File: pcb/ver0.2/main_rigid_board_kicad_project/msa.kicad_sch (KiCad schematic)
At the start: 37 parts, among them J1 USB_A, J2 SWD Prog, U1 MCP1702, U3 W25Q128JV, U4 RP2040, Y1 H130B-12.000-20-3050-EXT-TR

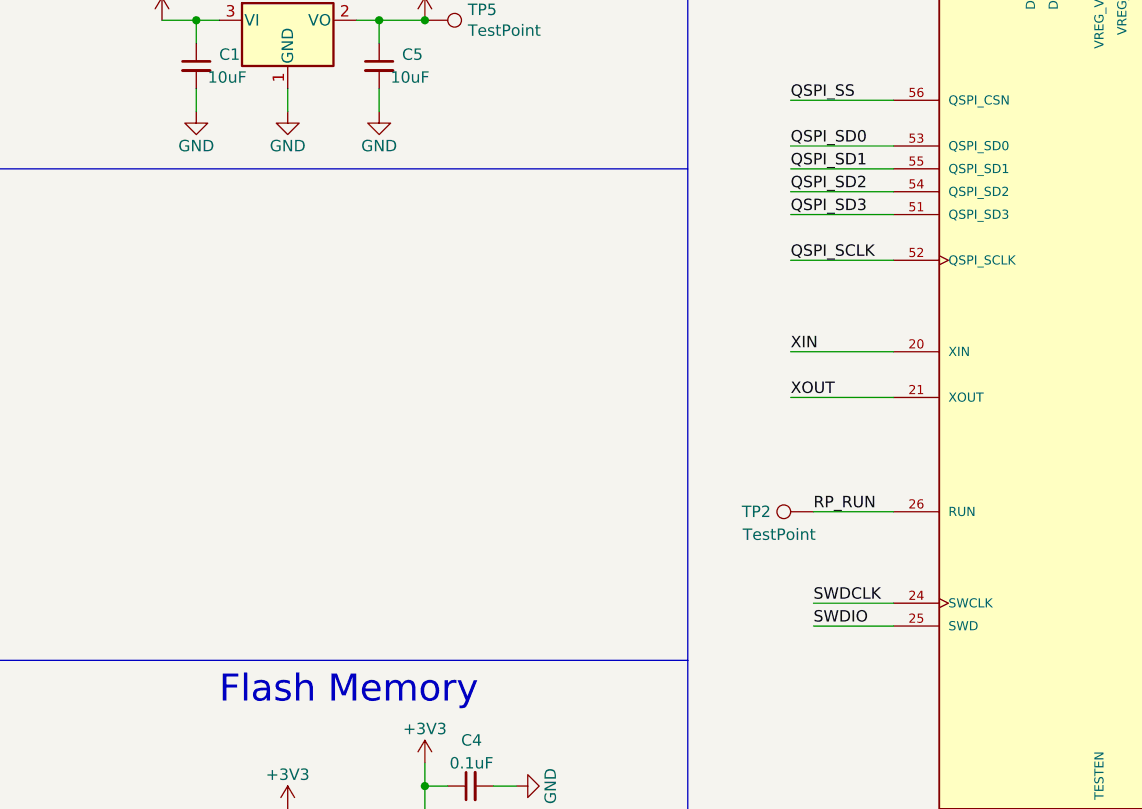
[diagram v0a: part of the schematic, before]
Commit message: add slimstack receptacle to library, add to main rigid board
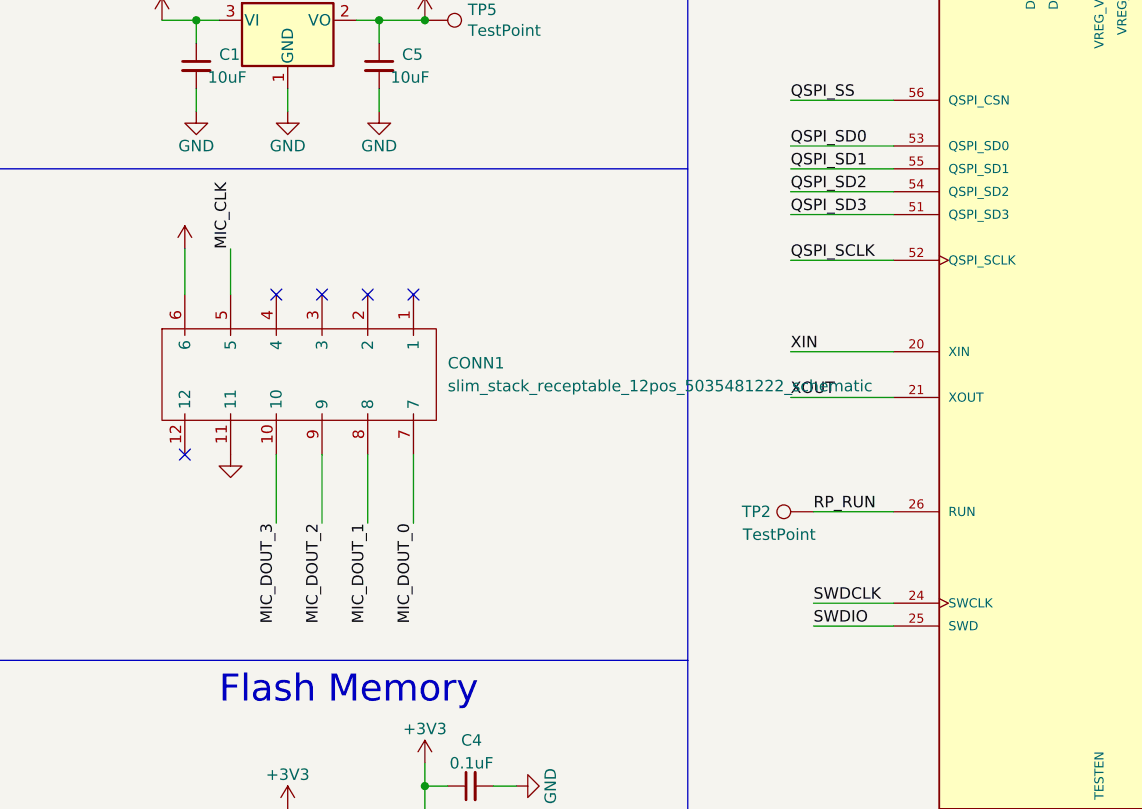
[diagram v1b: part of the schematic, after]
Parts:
- added CONN1: slim_stack_receptable_12pos_5035481222_schematic, OpenSourceSmartGlasses:slim_stack_molex_PLUG_5035521222, symbol MSA_lib:slim_stack_receptable_12pos_5035481222_schematic
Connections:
- net +3V3: now also CONN1.6
- net GND: now also CONN1.11
- net MIC_CLK: now also CONN1.5
- net MIC_DOUT_0: now also CONN1.7
- net MIC_DOUT_1: now also CONN1.8
- net MIC_DOUT_2: now also CONN1.9
- net MIC_DOUT_3: now also CONN1.10
- no-connect marks 24 -> 29
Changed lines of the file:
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@@
   (no_connect (at 182.88 105.41))
   (no_connect (at 182.88 130.81))
+  (no_connect (at 38.1 119.38))
   (no_connect (at 182.88 120.65))
   (no_connect (at 182.88 135.89))
   (no_connect (at 182.88 110.49))
+  (no_connect (at 63.5 101.6))
+  (no_connect (at 48.26 101.6))
+  (no_connect (at 58.42 101.6))
+  (no_connect (at 53.34 101.6))
   (no_connect (at 182.88 153.67))
   (no_connect (at 182.88 80.01))
@@
     (stroke (width 0) (type default) (color 0 0 0 0))
   )
+  (wire (pts (xy 63.5 119.38) (xy 63.5 127))
+    (stroke (width 0) (type default) (color 0 0 0 0))
+  )
   (polyline (pts (xy 172.72 162.56) (xy 236.22 162.56))
     (stroke (width 0) (type default) (color 0 0 0 0))
@@
     (stroke (width 0) (type default) (color 0 0 0 0))
   )
+  (wire (pts (xy 53.34 119.38) (xy 53.34 127))
+    (stroke (width 0) (type default) (color 0 0 0 0))
+  )
   (wire (pts (xy 59.69 71.12) (xy 64.77 71.12))
     (stroke (width 0) (type default) (color 0 0 0 0))
@@
     (stroke (width 0) (type default) (color 0 0 0 0))
   )
+  (wire (pts (xy 38.1 96.52) (xy 38.1 101.6))
+    (stroke (width 0) (type default) (color 0 0 0 0))
+  )
   (wire (pts (xy 257.81 120.65) (xy 257.81 123.19))
     (stroke (width 0) (type default) (color 0 0 0 0))
@@
     (stroke (width 0) (type default) (color 0 0 0 0))
   )
+  (wire (pts (xy 43.18 96.52) (xy 43.18 101.6))
+    (stroke (width 0) (type default) (color 0 0 0 0))
+  )
   (wire (pts (xy 182.88 69.85) (xy 193.04 69.85))
     (stroke (width 0) (type default) (color 0 0 0 0))
@@
     (stroke (width 0) (type default) (color 0 0 0 0))
   )
+  (wire (pts (xy 48.26 119.38) (xy 48.26 127))
+    (stroke (width 0) (type default) (color 0 0 0 0))
+  )
   (wire (pts (xy 116.84 135.89) (xy 107.95 135.89))
     (stroke (width 0) (type default) (color 0 0 0 0))
@@
   )
   (wire (pts (xy 182.88 138.43) (xy 193.04 138.43))
+    (stroke (width 0) (type default) (color 0 0 0 0))
+  )
+  (wire (pts (xy 58.42 119.38) (xy 58.42 127))
     (stroke (width 0) (type default) (color 0 0 0 0))
   )
@@
     (effects (font (size 1.27 1.27)) (justify left bottom))
   )
+  (label "MIC_CLK" (at 43.18 96.52 90)
+    (effects (font (size 1.27 1.27)) (justify left bottom))
+  )
   (label "XIN" (at 271.78 113.03 180)
     (effects (font (size 1.27 1.27)) (justify right bottom))
@@
     (effects (font (size 1.27 1.27)) (justify left bottom))
   )
+  (label "MIC_DOUT_3" (at 48.26 127 270)
+    (effects (font (size 1.27 1.27)) (justify right bottom))
+  )
   (label "QSPI_SCLK" (at 105.41 97.79 0)
     (effects (font (size 1.27 1.27)) (justify left bottom))
@@
   (label "MIC_DOUT_3" (at 193.04 140.97 0)
     (effects (font (size 1.27 1.27)) (justify left bottom))
+  )
+  (label "MIC_DOUT_2" (at 53.34 127 270)
+    (effects (font (size 1.27 1.27)) (justify right bottom))
   )
   (label "RED_LED" (at 194.31 133.35 180)
@@
     (effects (font (size 1.27 1.27)) (justify right bottom))
   )
+  (label "MIC_DOUT_1" (at 58.42 127 270)
+    (effects (font (size 1.27 1.27)) (justify right bottom))
+  )
   (label "MIC_CLK" (at 193.04 105.41 180)
     (effects (font (size 1.27 1.27)) (justify right bottom))
@@
   (label "SWDCLK" (at 251.46 83.82 0)
     (effects (font (size 1.27 1.27)) (justify left bottom))
+  )
+  (label "MIC_DOUT_0" (at 63.5 127 270)
+    (effects (font (size 1.27 1.27)) (justify right bottom))
   )
   (label "QSPI_SD0" (at 88.9 166.37 180)
@@
     (pin "1")
   )
+  (symbol (lib_name "GND_1") (lib_id "power:GND") (at 43.18 119.38 0) (unit 1)
+    (in_bom yes) (on_board yes) (fields_autoplaced)
+    (property "Reference" "#PWR05" (id 0) (at 43.18 125.73 0)
+      (effects (font (size 1.27 1.27)) hide)
+    )
+    (property "Value" "" (id 1) (at 43.18 124.46 0))
+    (property "Footprint" "" (id 2) (at 43.18 119.38 0)
+      (effects (font (size 1.27 1.27)) hide)
+    )
+    (property "Datasheet" "" (id 3) (at 43.18 119.38 0)
+      (effects (font (size 1.27 1.27)) hide)
+    )
+    (pin "1")
+  )
+  (symbol (lib_id "MSA_lib:slim_stack_receptable_12pos_5035481222_schematic") (at 44.45 107.95 0) (unit 1)
+    (in_bom yes) (on_board yes) (fields_autoplaced)
+    (property "Reference" "CONN1" (id 0) (at 67.31 109.2199 0)
+      (effects (font (size 1.27 1.27)) (justify left))
+    )
+    (property "Value" "slim_stack_receptable_12pos_5035481222_schematic" (id 1) (at 67.31 111.7599 0)
+      (effects (font (size 1.27 1.27)) (justify left))
+    )
+    (property "Footprint" "OpenSourceSmartGlasses:slim_stack_molex_PLUG_5035521222" (id 2) (at 45.72 92.71 0)
+      (effects (font (size 1.27 1.27)) hide)
+    )
+    (property "Datasheet" "" (id 3) (at 66.04 102.87 0)
+      (effects (font (size 1.27 1.27)) hide)
+    )
+    (pin "1")
+    (pin "10")
+    (pin "11")
+    (pin "12")
+    (pin "2")
+    (pin "3")
+    (pin "4")
+    (pin "5")
+    (pin "6")
+    (pin "7")
+    (pin "8")
+    (pin "9")
+  )
+  (symbol (lib_name "+3V3_1") (lib_id "power:+3V3") (at 38.1 96.52 0) (unit 1)
+    (in_bom yes) (on_board yes) (fields_autoplaced)
+    (property "Reference" "#PWR02" (id 0) (at 38.1 100.33 0)
+      (effects (font (size 1.27 1.27)) hide)
+    )
+    (property "Value" "" (id 1) (at 38.1 91.44 0))
+    (property "Footprint" "" (id 2) (at 38.1 96.52 0)
+      (effects (font (size 1.27 1.27)) hide)
+    )
+    (property "Datasheet" "" (id 3) (at 38.1 96.52 0)
+      (effects (font (size 1.27 1.27)) hide)
+    )
+    (pin "1")
+  )
   (sheet_instances
     (path "/" (page "1"))
@@
       (reference "#PWR01") (unit 1) (value "GND") (footprint "")
     )
+    (path "/9cfbbaab-6ac8-4331-b78f-216f7f09792d"
+      (reference "#PWR02") (unit 1) (value "+3V3") (footprint "")
+    )
     (path "/00000000-0000-0000-0000-000061fe1576"
       (reference "#PWR03") (unit 1) (value "VBUS") (footprint "")
@@
       (reference "#PWR04") (unit 1) (value "GND") (footprint "")
     )
+    (path "/285ee475-43b6-42c0-af90-9a0a6de0dadc"
+      (reference "#PWR05") (unit 1) (value "GND") (footprint "")
+    )
     (path "/00000000-0000-0000-0000-000061eec616"
       (reference "#PWR06") (unit 1) (value "GND") (footprint "")
@@
       (reference "C19") (unit 1) (value "27pF") (footprint "Capacitor_SMD:C_0402_1005Metric")
     )
+    (path "/2b3f38bb-dc91-41db-88d5-8b07790a4f71"
+      (reference "CONN1") (unit 1) (value "slim_stack_receptable_12pos_5035481222_schematic") (footprint "OpenSourceSmartGlasses:slim_stack_molex_PLUG_5035521222")
+    )
     (path "/00000000-0000-0000-0000-000061b9072f"

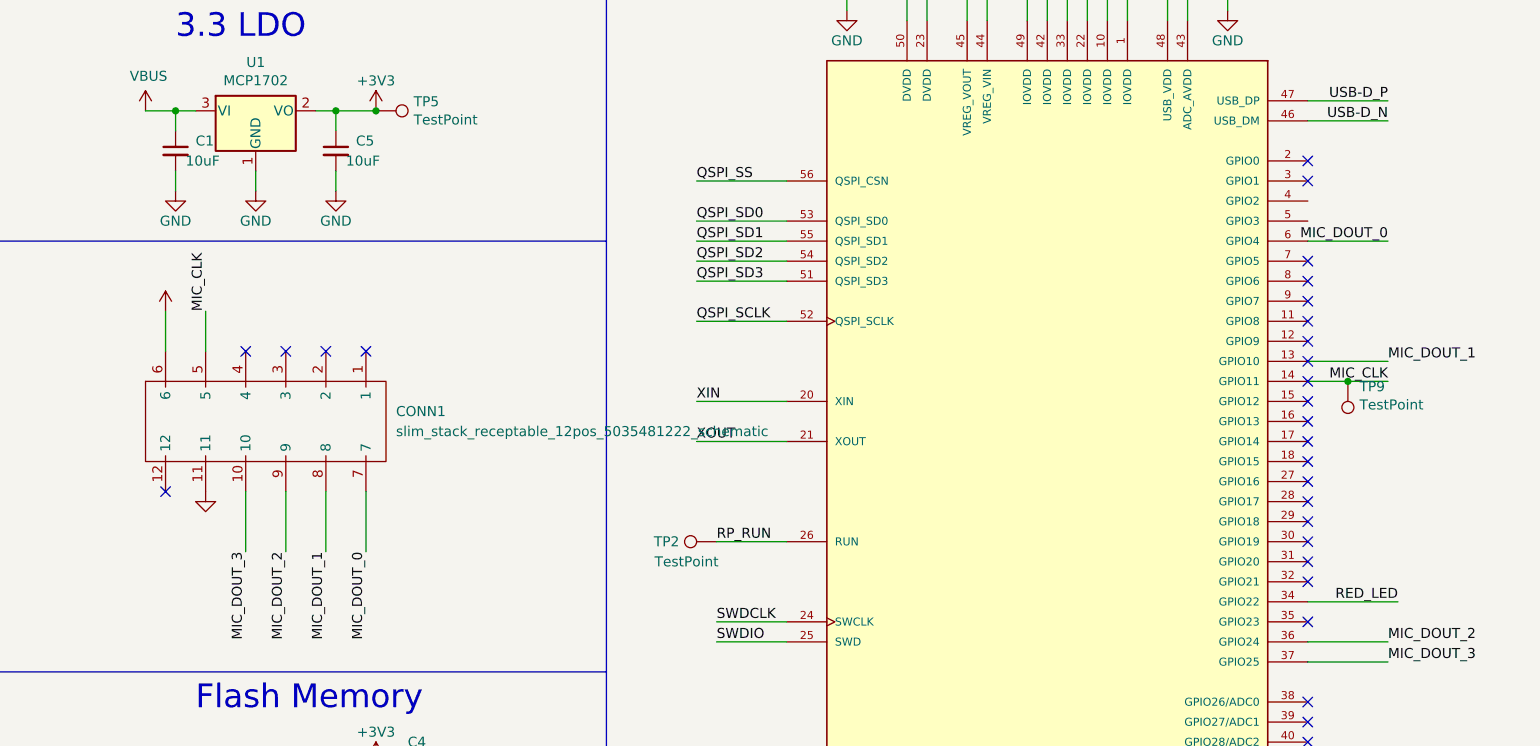
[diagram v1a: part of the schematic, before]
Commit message: finish implementing slim stacks, add stiffeners to flex pcb, run DRC and fix all issues on both boards
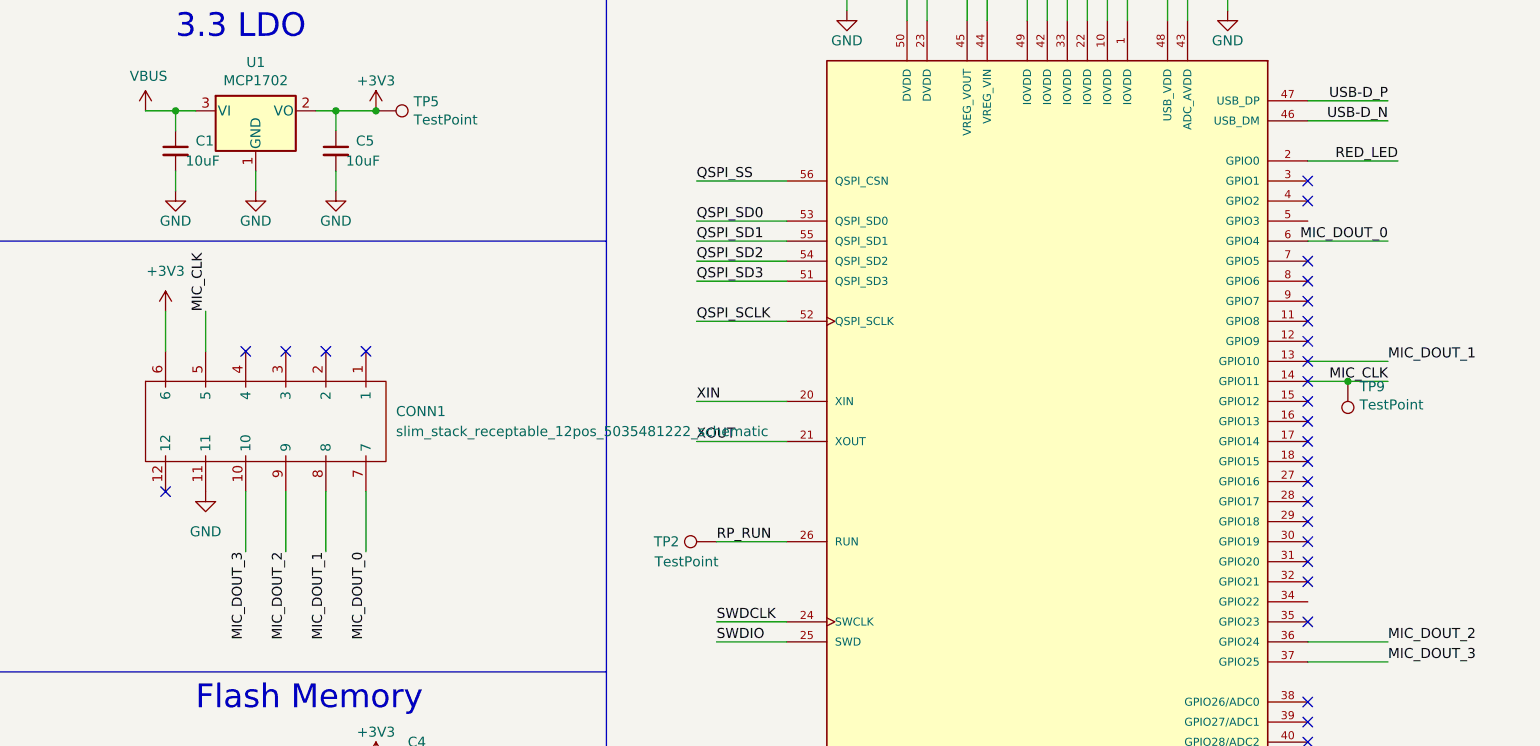
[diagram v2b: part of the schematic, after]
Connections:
- net RED_LED: now also U4.2 (GPIO0); no longer U4.34 (GPIO22)
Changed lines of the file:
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@@
   (no_connect (at 182.88 151.13))
   (no_connect (at 182.88 97.79))
-  (no_connect (at 182.88 77.47))
   (no_connect (at 182.88 90.17))
   (no_connect (at 182.88 148.59))
@@
   (no_connect (at 53.34 101.6))
   (no_connect (at 182.88 153.67))
-  (no_connect (at 182.88 80.01))
   (no_connect (at 182.88 113.03))
   (no_connect (at 182.88 128.27))
+  (no_connect (at 182.88 82.55))
   (no_connect (at 182.88 95.25))
   (no_connect (at 182.88 102.87))
@@
   (no_connect (at 182.88 107.95))
   (no_connect (at 182.88 125.73))
+  (no_connect (at 182.88 80.01))
   (polyline (pts (xy 172.72 193.04) (xy 172.72 162.56))
     (stroke (width 0) (type default) (color 0 0 0 0))
@@
     (stroke (width 0) (type default) (color 0 0 0 0))
   )
-  (wire (pts (xy 194.31 133.35) (xy 182.88 133.35))
-    (stroke (width 0) (type default) (color 0 0 0 0))
-  )
   (wire (pts (xy 134.62 53.34) (xy 139.7 53.34))
     (stroke (width 0) (type default) (color 0 0 0 0))
@@
   )
   (wire (pts (xy 255.27 118.11) (xy 247.65 118.11))
+    (stroke (width 0) (type default) (color 0 0 0 0))
+  )
+  (wire (pts (xy 194.31 77.47) (xy 182.88 77.47))
     (stroke (width 0) (type default) (color 0 0 0 0))
   )
@@
     (effects (font (size 1.27 1.27)) (justify right bottom))
   )
-  (label "RED_LED" (at 194.31 133.35 180)
-    (effects (font (size 1.27 1.27)) (justify right bottom))
-  )
   (label "MIC_DOUT_0" (at 193.04 87.63 180)
     (effects (font (size 1.27 1.27)) (justify right bottom))
@@
   (label "XOUT" (at 105.41 113.03 0)
     (effects (font (size 1.27 1.27)) (justify left bottom))
+  )
+  (label "RED_LED" (at 194.31 77.47 180)
+    (effects (font (size 1.27 1.27)) (justify right bottom))
   )
   (label "SWDCLK" (at 251.46 83.82 0)
@@
       (effects (font (size 1.27 1.27)) hide)
     )
-    (property "Value" "" (id 1) (at 43.18 124.46 0))
+    (property "Value" "GND" (id 1) (at 43.18 124.46 0))
     (property "Footprint" "" (id 2) (at 43.18 119.38 0)
       (effects (font (size 1.27 1.27)) hide)
@@
       (effects (font (size 1.27 1.27)) hide)
     )
-    (property "Value" "" (id 1) (at 38.1 91.44 0))
+    (property "Value" "+3V3" (id 1) (at 38.1 91.44 0))
     (property "Footprint" "" (id 2) (at 38.1 96.52 0)
       (effects (font (size 1.27 1.27)) hide)

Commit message: add LiPo battery management circuit
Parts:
- added BT1: (no value), symbol Device:Battery_Cell
- added C2, C20, C3: (no value), symbol Device:C_Small
- added D2: (no value), symbol Device:LED
- added D3: (no value), symbol Diode:BAT60A
- added Q1: (no value), symbol Transistor_FET:DMP3013SFV
- added R1, R8, R9: (no value), symbol Device:R_Small
- added U2: (no value), symbol Battery_Management:MCP73831-2-OT
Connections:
- net VBUS: now also C3.1, D3.2 (A), Q1.4 (G), R1.2, R9.1, U2.4 (VDD); no longer C1.1, U1.3 (VI)
- net GND renamed -BATT
- net -BATT: now also BT1.2 (-), C2.2, C20.2, C3.2, R8.2, R9.2, U2.2 (VSS)
- new net: D2.1 (K), U2.1 (STAT)
- new net: D2.2 (A), R1.1
- new net: R8.1, U2.5 (PROG)
- new net +BATT: BT1.1 (+), C2.1, Q1.5 (D), U2.3 (VBAT)
- new net +VDC: C1.1, C20.1, D3.1 (K), Q1.1 (S), Q1.2 (S), Q1.3 (S), U1.3 (VI)
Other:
- note added: "Li-Po Charging"
- note added: "Li-Po Load Sharing"
- note added: "LiPo Battery"

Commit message: last changes setup for manufacturing for v0p2 - only step left is spacing of microphones
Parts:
- removed D3: (no value), symbol Diode:BAT60A
- removed J1: USB_A, Connector_USB:USB_Micro-B_Molex-105133-0001, symbol mico-rescue:USB_A-Connector
- removed Q1: (no value), symbol Transistor_FET:DMP3013SFV
- added D3: (no value), symbol Diode:PMEG2010AEJ
- added J1: (no value), symbol Connector:USB_B_Micro
- added R10: (no value), symbol Device:R_Small
- added U5: (no value), Package_TO_SOT_SMD:SOT-523, symbol MSA_lib:‎DMP21D0UT-7‎
- C2, C3: value (none) -> 4.7uF; footprint (none) -> Capacitor_SMD:C_0402_1005Metric_Pad0.74x0.62mm_HandSolder
- C20: value (none) -> 1uF; footprint (none) -> Capacitor_SMD:C_0402_1005Metric_Pad0.74x0.62mm_HandSolder
- D2: value (none) -> LED; footprint (none) -> Capacitor_SMD:C_0402_1005Metric_Pad0.74x0.62mm_HandSolder
- R1: value (none) -> 470; footprint (none) -> Capacitor_SMD:C_0402_1005Metric_Pad0.74x0.62mm_HandSolder
- R8: value (none) -> 10k; footprint (none) -> Capacitor_SMD:C_0402_1005Metric_Pad0.74x0.62mm_HandSolder
- R9: value (none) -> 100k; footprint (none) -> Capacitor_SMD:C_0402_1005Metric_Pad0.74x0.62mm_HandSolder
- U2: value (none) -> MCP73831-2-OT; footprint (none) -> Package_TO_SOT_SMD:SOT-23-5
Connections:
- net +BATT: now also U5.3 (D)
- net +VDC: now also D3.1 (K), R10.2, U5.2 (S)
- net -BATT: now also J1.5 (GND), J1.6 (Shield)
- net USB0-D_N: now also J1.2 (D-)
- net USB0-D_P: now also J1.3 (D+)
- net VBUS: now also D3.2 (A), J1.1 (VBUS), R10.1, U5.1 (G)
- no-connect marks 29 -> 30
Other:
- note added: "NC 0hm in case our battery charge circuit doesn't work as expected"
